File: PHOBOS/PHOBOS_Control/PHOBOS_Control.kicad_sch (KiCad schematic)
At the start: 43 parts, among them J1 Screw_Terminal_01x02, J4 USB Boot, J6 USB4056-03-A_REVA2, SW4 KMR211GLFS, U3 W25Q128JVSIQ, U4 NCP1117-3.3_SOT223, U5 RP2040, Y1 ABM8-272-T3

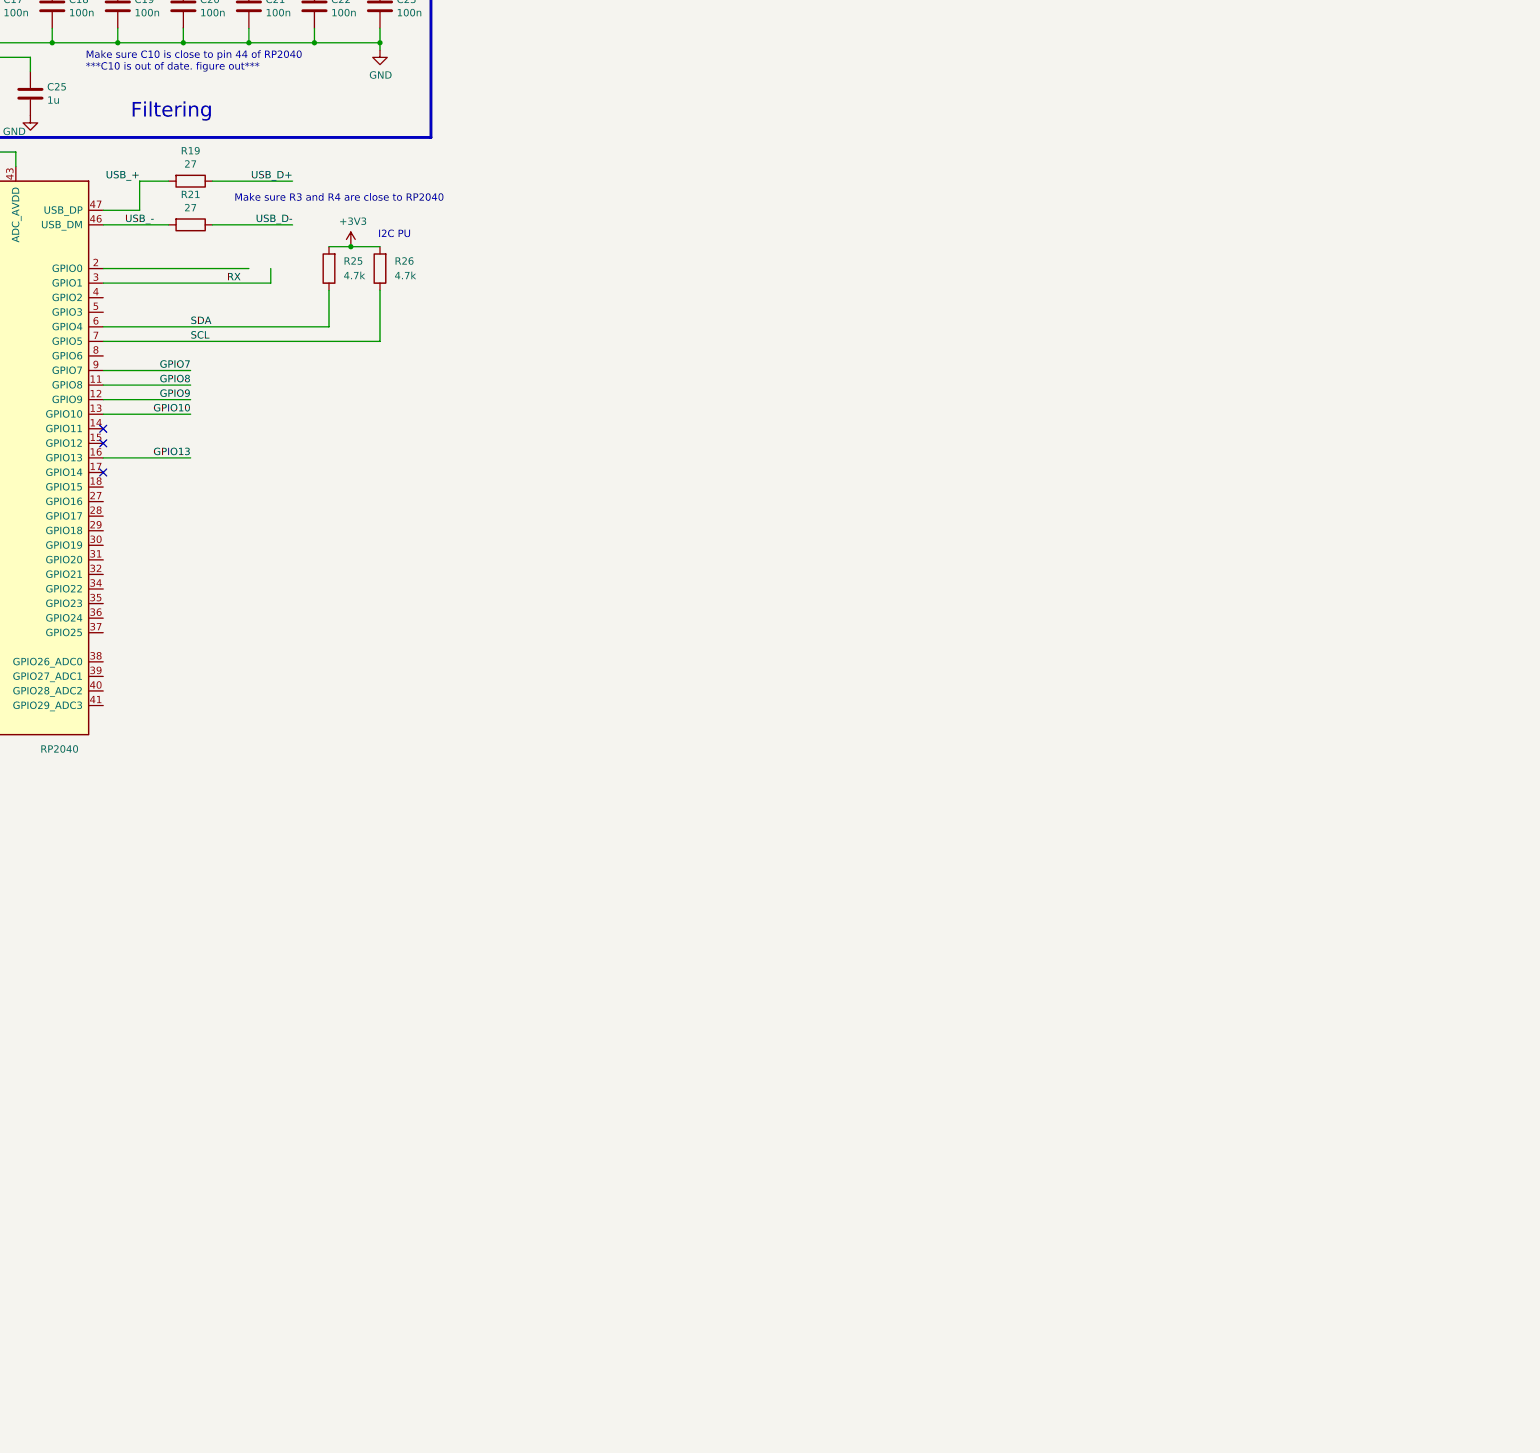
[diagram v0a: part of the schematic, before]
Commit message: Transceiver circuit added, op amp and connector added.
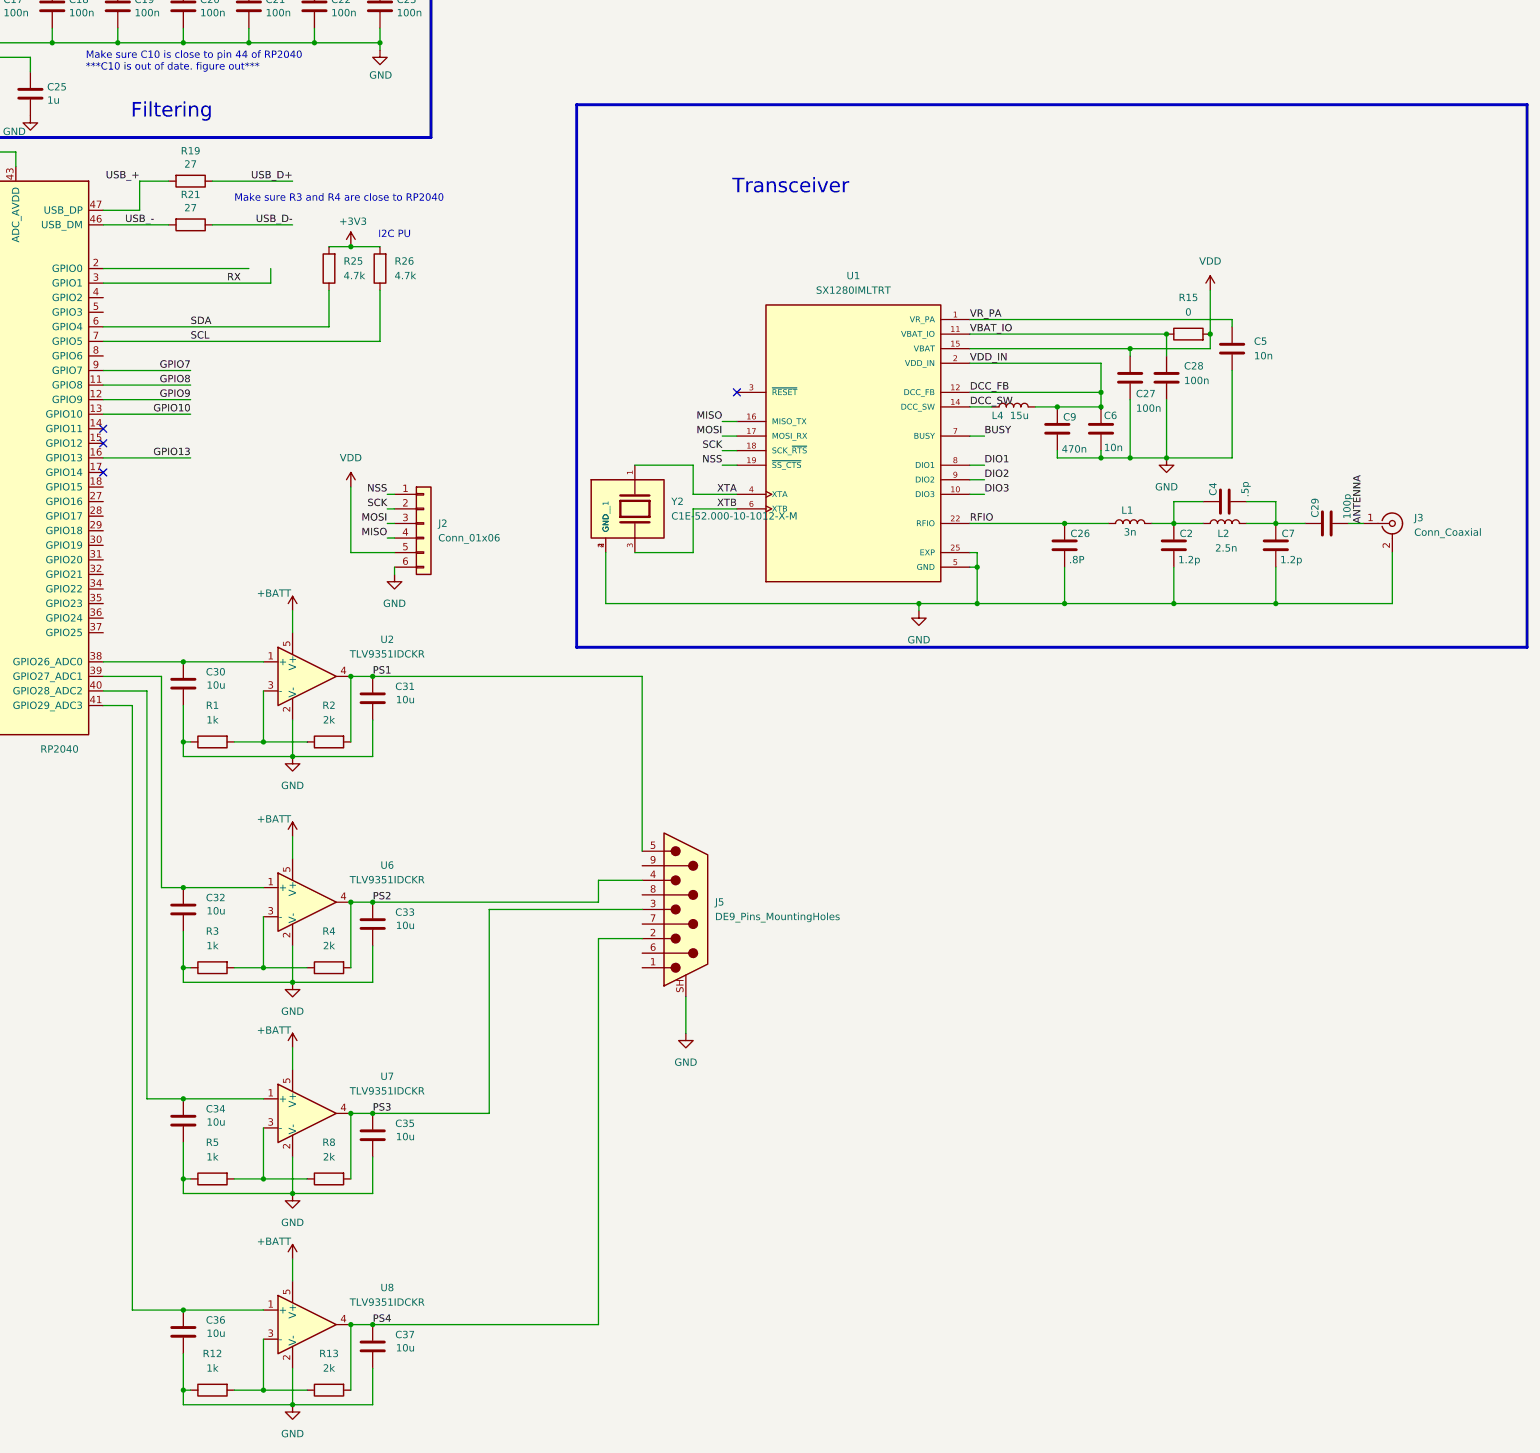
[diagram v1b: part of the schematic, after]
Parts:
- added C2, C7: 1.2p, Capacitor_SMD:C_0402_1005Metric_Pad0.74x0.62mm_HandSolder, symbol Device:C
- added C26: .8P, Capacitor_SMD:C_0402_1005Metric_Pad0.74x0.62mm_HandSolder, symbol Device:C
- added C27, C28: 100n, Capacitor_SMD:C_0402_1005Metric_Pad0.74x0.62mm_HandSolder, symbol Device:C
- added C29: 100p, Capacitor_SMD:C_0402_1005Metric_Pad0.74x0.62mm_HandSolder, symbol Device:C
- added C30, C31, C32, C33, C34, C35, C36, C37: 10u, Capacitor_SMD:C_0402_1005Metric, symbol Device:C
- added C4: .5p, Capacitor_SMD:C_0402_1005Metric_Pad0.74x0.62mm_HandSolder, symbol Device:C
- added C5, C6: 10n, Capacitor_SMD:C_0402_1005Metric_Pad0.74x0.62mm_HandSolder, symbol Device:C
- added C9: 470n, Capacitor_SMD:C_0402_1005Metric_Pad0.74x0.62mm_HandSolder, symbol Device:C
- added J2: Conn_01x06, Connector_PinHeader_2.54mm:PinHeader_1x06_P2.54mm_Vertical, symbol Connector_Generic:Conn_01x06
- added J3: Conn_Coaxial, Connector_Coaxial:SMA_Amphenol_132134-10_Vertical, symbol Connector:Conn_Coaxial
- added J5: DE9_Pins_MountingHoles, Connector_Dsub:DSUB-9_Pins_Horizontal_P2.77x2.84mm_EdgePinOffset7.70mm_Housed_MountingHolesOffset9.12mm, symbol Connector:DE9_Pins_MountingHoles
- added L1: 3n, Inductor_SMD:L_0402_1005Metric_Pad0.77x0.64mm_HandSolder, symbol Device:L
- added L2: 2.5n, Inductor_SMD:L_0402_1005Metric_Pad0.77x0.64mm_HandSolder, symbol Device:L
- added L4: 15u, Inductor_SMD:L_0805_2012Metric_Pad1.05x1.20mm_HandSolder, symbol Device:L
- added R1, R12, R3, R5: 1k, symbol Device:R
- added R13, R2, R4, R8: 2k, symbol Device:R
- added R15: 0, Resistor_SMD:R_0402_1005Metric_Pad0.72x0.64mm_HandSolder, symbol Device:R
- added U1: SX1280IMLTRT, SX1280IMLTRT:XCVR_SX1280IMLTRT, symbol SX1280IMLTRT:SX1280IMLTRT
- added U2, U6, U7, U8: TLV9351IDCKR, Package_TO_SOT_SMD:SOT-353_SC-70-5, symbol Amplifier_Operational:TLV172IDCK
- added Y2: C1E-52.000-10-1012-X-M, C1E-52.000-10-1012-X-M:XTAL_C1E-52.000-10-1012-X-M, symbol C1E-52.000-10-1012-X-M:C1E-52.000-10-1012-X-M
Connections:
- net +BATT: now also U2.5 (V+), U6.5 (V+), U7.5 (V+), U8.5 (V+)
- net GND: now also C2.2, C26.2, C27.2, C28.2, C30.2, C31.2, C32.2, C33.2, C34.2, C35.2, C36.2, C37.2, C5.2, C6.2, C7.2, C9.2, J2.6 (Pin_6), J3.2 (Ext), J5.SH (PAD), R1.1, R12.1, R3.1, R5.1, U1.13 (GND), U1.20 (GND), U1.21 (GND), U1.23 (GND), U1.24 (GND), U1.25 (EXP), U1.5 (GND), U2.2 (V-), U6.2 (V-), U7.2 (V-), U8.2 (V-), Y2.2 (GND), Y2.4 (GND__1)
- net at U5.38 (GPIO26_ADC0): now also C30.1, U2.1 (+)
- net at U5.39 (GPIO27_ADC1): now also C32.1, U6.1 (+)
- net at U5.40 (GPIO28_ADC2): now also C34.1, U7.1 (+)
- net at U5.41 (GPIO29_ADC3): now also C36.1, U8.1 (+)
- new net: C2.1, C4.1, L1.2, L2.1
- new net: C29.1, C4.2, C7.1, L2.2
- new net: R3.2, R4.1, U6.3 (-)
- new net: R12.2, R13.1, U8.3 (-)
- new net: R5.2, R8.1, U7.3 (-)
- new net: R1.2, R2.1, U2.3 (-)
- new net ANTENNA: C29.2, J3.1 (In)
- new net BUSY: U1.7 (BUSY)
- new net DCC_FB: C6.1, C9.1, L4.2, U1.12 (DCC_FB), U1.2 (VDD_IN)
- new net DCC_SW: L4.1, U1.14 (DCC_SW)
- new net DIO1: U1.8 (DIO1)
- new net DIO2: U1.9 (DIO2)
- new net DIO3: U1.10 (DIO3)
- new net MISO: J2.4 (Pin_4), U1.16 (MISO_TX)
- new net MOSI: J2.3 (Pin_3), U1.17 (MOSI_RX)
- new net NSS: J2.1 (Pin_1), U1.19 (~{SS_CTS})
- new net PS1: C31.1, J5.5, R2.2, U2.4
- new net PS2: C33.1, J5.4, R4.2, U6.4
- new net PS3: C35.1, J5.3, R8.2, U7.4
- new net PS4: C37.1, J5.2, R13.2, U8.4
- new net RFIO: C26.1, L1.1, U1.22 (RFIO)
- new net SCK: J2.2 (Pin_2), U1.18 (SCK_~{RTS})
- new net VBAT_IO: C28.1, R15.1, U1.11 (VBAT_IO)
- new net VDD: C27.1, J2.5 (Pin_5), R15.2, U1.15 (VBAT)
- new net VR_PA: C5.1, U1.1 (VR_PA)
- new net XTA: U1.4 (XTA), Y2.1
- new net XTB: U1.6 (XTB), Y2.3
- no-connect marks 13 -> 14
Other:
- note added: "Transceiver"

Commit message: Parts updated, all footprints available.
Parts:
- added J7: SMA-J-P-GF-RA-SM1, SMA-J-P-GF-RA-SM1:SAMTEC_SMA-J-P-GF-RA-SM1, symbol SMA_J_P_GF_RA_SM1:SMA-J-P-GF-RA-SM1
- J3: footprint Connector_Coaxial:SMA_Amphenol_132134-10_Vertical -> SMA_J_P_GF_RA_SM1:SAMTEC_SMA-J-P-GF-RA-SM1
- J6: footprint USB4056-03-A:GCT_USB4056-03-A_REVA2 -> USB4056_03_A:GCT_USB4056-03-A_REVA2
- R1, R12, R13, R2, R3, R4, R5, R8: footprint (none) -> Resistor_SMD:R_0402_1005Metric_Pad0.72x0.64mm_HandSolder
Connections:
- net GND: now also J3.3 (Ext), J3.4 (Ext), J3.5 (Ext)
- new net: J7.2, J7.3, J7.4, J7.5
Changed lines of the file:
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@@
 	)
 	(symbol
+		(lib_id "SMA_J_P_GF_RA_SM1:SMA-J-P-GF-RA-SM1")
+		(at 551.18 222.25 0)
+		(unit 1)
+		(body_style 1)
+		(exclude_from_sim no)
+		(in_bom yes)
+		(on_board yes)
+		(in_pos_files yes)
+		(dnp no)
+		(fields_autoplaced yes)
+		(property "Reference" "J7"
+			(at 550.799 213.36 0)
+			(show_name no)
+			(do_not_autoplace no)
+			(effects
+				(font
+					(size 1.27 1.27)
+				)
+			)
+		)
+		(property "Value" "SMA-J-P-GF-RA-SM1"
+			(at 550.799 215.9 0)
+			(show_name no)
+			(do_not_autoplace no)
+			(effects
+				(font
+					(size 1.27 1.27)
+				)
+			)
+		)
+		(property "Footprint" "SMA-J-P-GF-RA-SM1:SAMTEC_SMA-J-P-GF-RA-SM1"
+			(at 551.18 222.25 0)
+			(hide yes)
+			(show_name no)
+			(do_not_autoplace no)
+			(effects
+				(font
+					(size 1.27 1.27)
+				)
+				(justify bottom)
+			)
+		)
+		(property "Datasheet" ""
+			(at 551.18 222.25 0)
+			(hide yes)
+			(show_name no)
+			(do_not_autoplace no)
+			(effects
+				(font
+					(size 1.27 1.27)
+				)
+			)
+		)
+		(property "Description" ""
+			(at 551.18 222.25 0)
+			(hide yes)
+			(show_name no)
+			(do_not_autoplace no)
+			(effects
+				(font
+					(size 1.27 1.27)
+				)
+			)
+		)
+		(property "PARTREV" "D"
+			(at 551.18 222.25 0)
+			(hide yes)
+			(show_name no)
+			(do_not_autoplace no)
+			(effects
+				(font
+					(size 1.27 1.27)
+				)
+				(justify bottom)
+			)
+		)
+		(property "MANUFACTURER" "Samtec"
+			(at 551.18 222.25 0)
+			(hide yes)
+			(show_name no)
+			(do_not_autoplace no)
+			(effects
+				(font
+					(size 1.27 1.27)
+				)
+				(justify bottom)
+			)
+		)
+		(property "MAXIMUM_PACKAGE_HEIGHT" "9.99mm"
+			(at 551.18 222.25 0)
+			(hide yes)
+			(show_name no)
+			(do_not_autoplace no)
+			(effects
+				(font
+					(size 1.27 1.27)
+				)
+				(justify bottom)
+			)
+		)
+		(property "STANDARD" "Manufacturer Recommendations"
+			(at 551.18 222.25 0)
+			(hide yes)
+			(show_name no)
+			(do_not_autoplace no)
+			(effects
+				(font
+					(size 1.27 1.27)
+				)
+				(justify bottom)
+			)
+		)
+		(pin "4"
+		)
+		(pin "1"
+		)
+		(pin "2"
+		)
+		(pin "3"
+		)
+		(pin "5"
+		)
+		(instances
+			(project "PHOBOS_Control"
+				(path "/311bc0a8-e09e-4ed9-a164-96f32995a395"
+					(reference "J7")
+					(unit 1)
+				)
+			)
+		)
+	)
+	(symbol
 		(lib_id "Device:C")
 		(at 309.88 143.51 0)
@@
 			)
 		)
-		(property "Footprint" ""
+		(property "Footprint" "Resistor_SMD:R_0402_1005Metric_Pad0.72x0.64mm_HandSolder"
 			(at 337.82 383.032 90)
 			(hide yes)
@@
 			)
 		)
-		(property "Footprint" ""
+		(property "Footprint" "Resistor_SMD:R_0402_1005Metric_Pad0.72x0.64mm_HandSolder"
 			(at 358.14 309.372 90)
 			(hide yes)
@@
 			)
 		)
-		(property "Footprint" ""
+		(property "Footprint" "Resistor_SMD:R_0402_1005Metric_Pad0.72x0.64mm_HandSolder"
 			(at 337.82 309.372 90)
 			(hide yes)
@@
 			)
 		)
-		(property "Footprint" ""
+		(property "Footprint" "Resistor_SMD:R_0402_1005Metric_Pad0.72x0.64mm_HandSolder"
 			(at 337.82 346.202 90)
 			(hide yes)
@@
 			)
 		)
-		(property "Footprint" "Connector_Coaxial:SMA_Amphenol_132134-10_Vertical"
+		(property "Footprint" "SMA_J_P_GF_RA_SM1:SAMTEC_SMA-J-P-GF-RA-SM1"
 			(at 543.56 233.68 0)
 			(hide yes)
@@
 		(pin "1"
 		)
+		(pin "4"
+		)
+		(pin "5"
+		)
+		(pin "3"
+		)
 		(instances
 			(project "PHOBOS_Control"
@@
 			)
 		)
-		(property "Footprint" ""
+		(property "Footprint" "Resistor_SMD:R_0402_1005Metric_Pad0.72x0.64mm_HandSolder"
 			(at 358.14 346.202 90)
 			(hide yes)
@@
 			)
 		)
-		(property "Footprint" "USB4056-03-A:GCT_USB4056-03-A_REVA2"
+		(property "Footprint" "USB4056_03_A:GCT_USB4056-03-A_REVA2"
 			(at 128.27 119.38 0)
 			(hide yes)
@@
 			)
 		)
-		(property "Footprint" ""
+		(property "Footprint" "Resistor_SMD:R_0402_1005Metric_Pad0.72x0.64mm_HandSolder"
 			(at 358.14 270.002 90)
 			(hide yes)
@@
 			)
 		)
-		(property "Footprint" ""
+		(property "Footprint" "Resistor_SMD:R_0402_1005Metric_Pad0.72x0.64mm_HandSolder"
 			(at 337.82 270.002 90)
 			(hide yes)
@@
 			)
 		)
-		(property "Footprint" ""
+		(property "Footprint" "Resistor_SMD:R_0402_1005Metric_Pad0.72x0.64mm_HandSolder"
 			(at 358.14 383.032 90)
 			(hide yes)
